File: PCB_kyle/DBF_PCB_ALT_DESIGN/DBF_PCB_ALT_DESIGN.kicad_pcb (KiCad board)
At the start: 4 copper layers, 150 x 65 mm, 9 parts

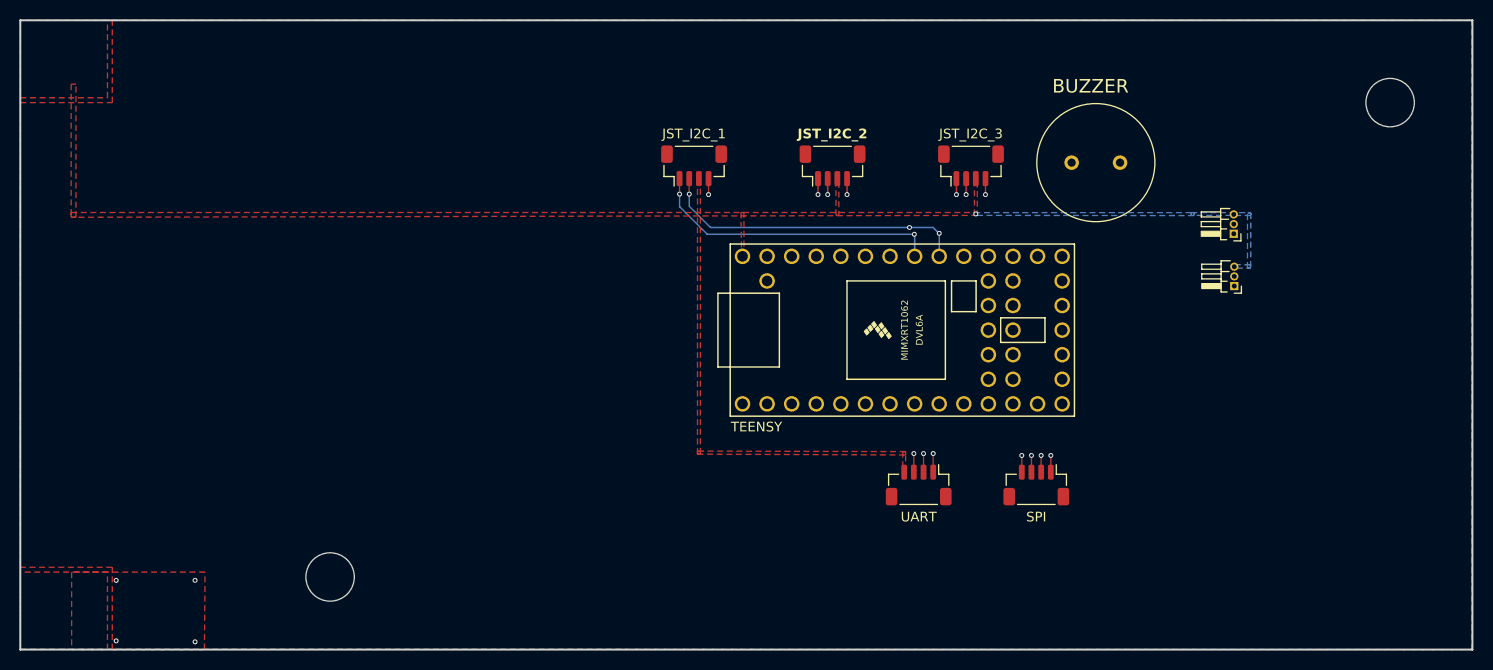
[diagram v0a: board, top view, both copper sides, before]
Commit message: Pin headers changed + no DRC errors, some warnings not too bad
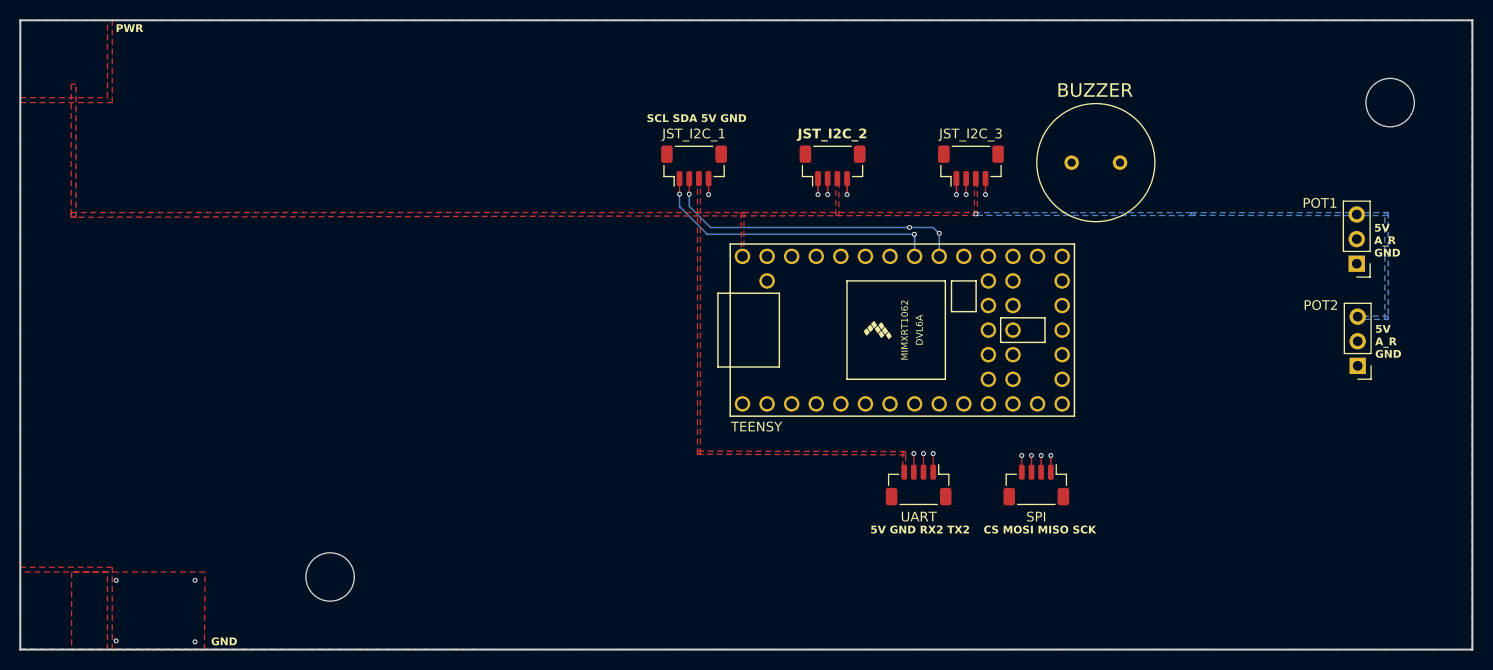
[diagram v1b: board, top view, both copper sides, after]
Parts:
- removed REF** (x2): PinHeader_1x03_P1.00mm_Horizontal, Connector_PinHeader_1.00mm:PinHeader_1x03_P1.00mm_Horizontal
- added POT1: POT1, Connector_PinHeader_2.54mm:PinHeader_1x03_P2.54mm_Vertical, F.Cu at (238.1, 75.1)
- added POT2: PinHeader_1x03_P2.54mm_Vertical, Connector_PinHeader_2.54mm:PinHeader_1x03_P2.54mm_Vertical, F.Cu at (238.2, 85.7)
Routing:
- net POT2: track 22.7 -> 38.0 mm
- net POT1: track 24.2 -> 37.0 mm
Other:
- board text added: "5V A_R GND"
- board text added: "5V GND RX2 TX2"
- board text added: "CS MOSI MISO SCK"
- board text added: "GND"
- board text added: "PWR"
- board text added: "SCL SDA 5V GND"
